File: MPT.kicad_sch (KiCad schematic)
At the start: 6 parts, among them SW1 OS102011MA1QN1

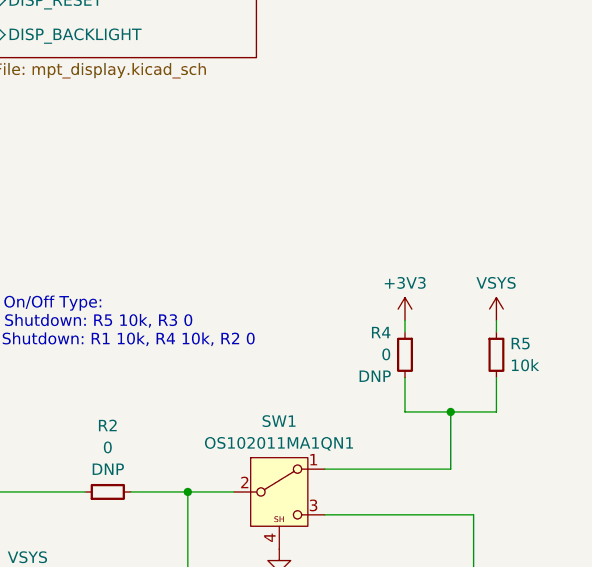
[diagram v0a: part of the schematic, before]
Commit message: Added Info-Table for STAT Pins and LEDS of Charger Work In Progress regulation for Display driving (currently not working)
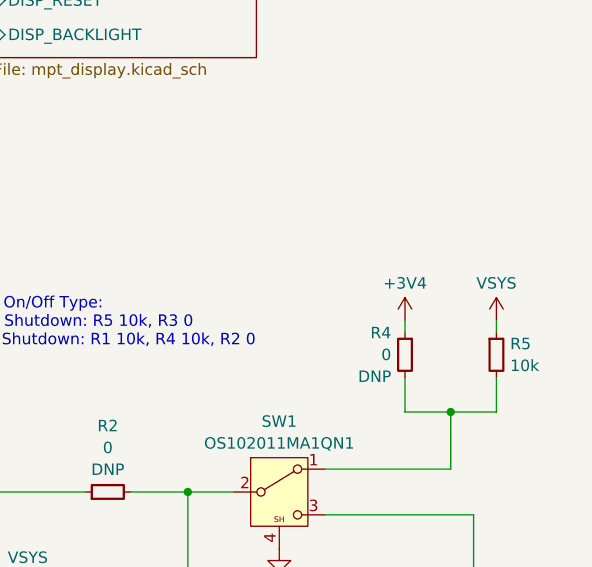
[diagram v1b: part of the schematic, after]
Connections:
- net +3V3 renamed +3V4
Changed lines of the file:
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@@
 			)
 		)
-		(property "Value" "+3V3"
+		(property "Value" "+3V4"
 			(at 228.6 86.0369 0)
 			(show_name no)

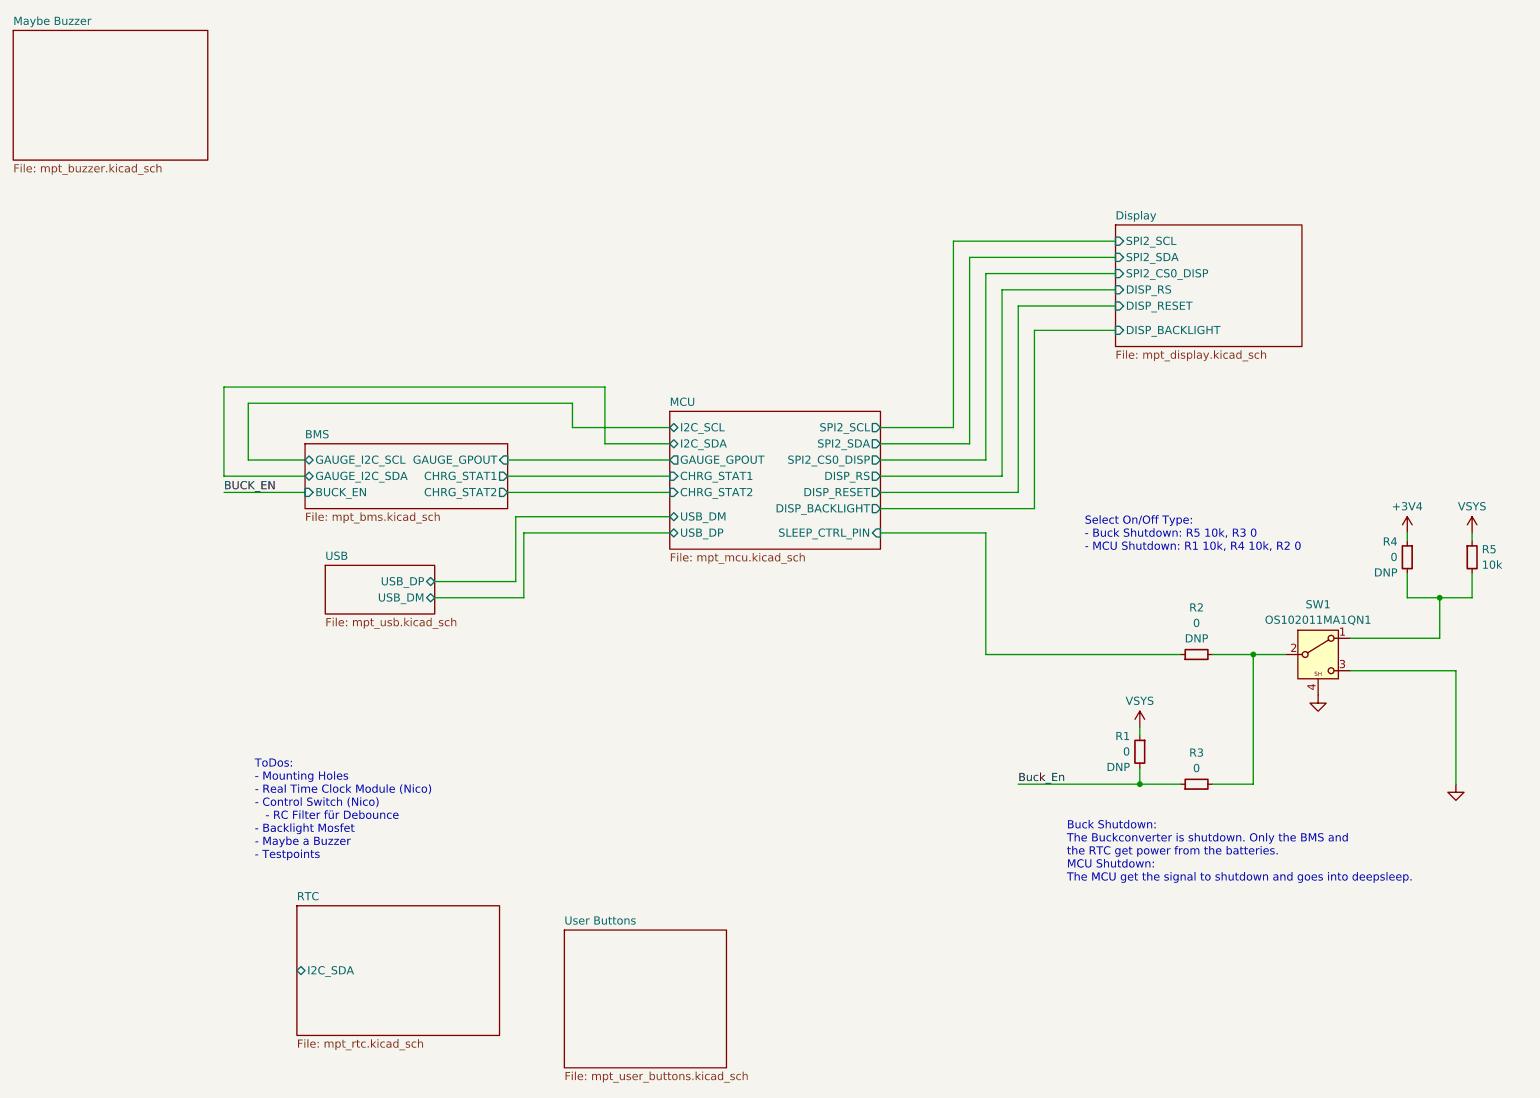
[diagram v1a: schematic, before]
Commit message: Changed LED Driver for one with lower Headroom
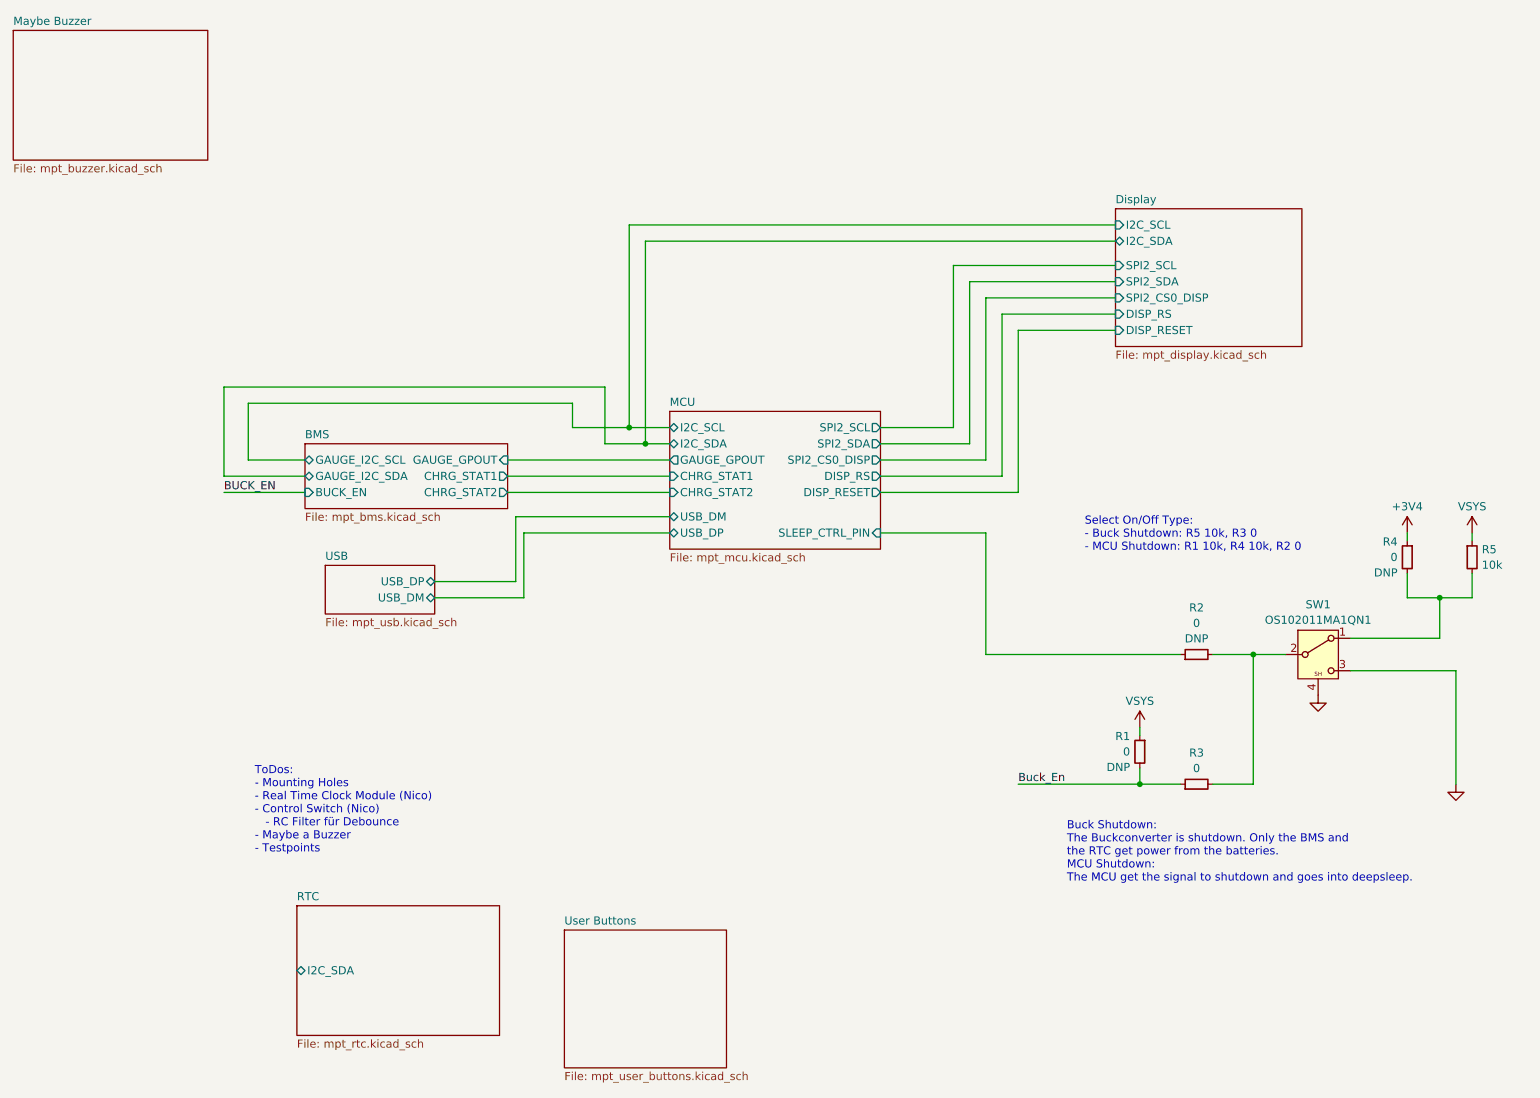
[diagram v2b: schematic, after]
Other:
- sheet Display ports: added I2C_SCL, I2C_SDA; removed DISP_BACKLIGHT
- sheet MCU ports: added none; removed DISP_BACKLIGHT
- note added: "ToDos: - Mounting Holes - Real Time Clock Module (Nico) - Control Switch (Nico) - RC Filter für Debounce - Maybe a Buzzer - Testpoints"
- note removed: "ToDos: - Mounting Holes - Real Time Clock Module (Nico) - Control Switch (Nico) - RC Filter für Debounce - Backlight Mosfet - Maybe a Buzzer - Testpoints"
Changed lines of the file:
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@@
 		)
 	)
-	(text "ToDos:\n- Mounting Holes\n- Real Time Clock Module (Nico)\n- Control Switch (Nico)\n   - RC Filter für Debounce\n- Backlight Mosfet\n- Maybe a Buzzer\n- Testpoints"
+	(text "ToDos:\n- Mounting Holes\n- Real Time Clock Module (Nico)\n- Control Switch (Nico)\n   - RC Filter für Debounce\n- Maybe a Buzzer\n- Testpoints"
 		(exclude_from_sim no)
 		(at 48.006 133.604 0)
@@
 		(color 0 0 0 0)
 	)
-	(wire
-		(pts
-			(xy 165.1 81.28) (xy 165.1 52.07)
+	(junction
+		(at 109.22 76.2)
+		(diameter 0)
+		(color 0 0 0 0)
+	)
+	(junction
+		(at 106.68 73.66)
+		(diameter 0)
+		(color 0 0 0 0)
+	)
+	(wire
+		(pts
+			(xy 165.1 81.28) (xy 165.1 55.88)
 		)
 		(stroke
@@
 	(wire
 		(pts
-			(xy 157.48 73.66) (xy 157.48 44.45)
+			(xy 157.48 73.66) (xy 157.48 48.26)
 		)
 		(stroke
@@
 	(wire
 		(pts
-			(xy 182.88 54.61) (xy 167.64 54.61)
+			(xy 182.88 58.42) (xy 167.64 58.42)
 		)
 		(stroke
@@
 	(wire
 		(pts
-			(xy 165.1 52.07) (xy 182.88 52.07)
+			(xy 165.1 55.88) (xy 182.88 55.88)
 		)
 		(stroke
@@
 	(wire
 		(pts
+			(xy 182.88 41.91) (xy 106.68 41.91)
+		)
+		(stroke
+			(width 0)
+			(type default)
+		)
+	)
+	(wire
+		(pts
 			(xy 198.12 129.54) (xy 204.47 129.54)
 		)
@@
 	(wire
 		(pts
-			(xy 162.56 78.74) (xy 162.56 49.53)
+			(xy 162.56 78.74) (xy 162.56 53.34)
 		)
 		(stroke
@@
 	(wire
 		(pts
-			(xy 160.02 46.99) (xy 182.88 46.99)
-		)
-		(stroke
-			(width 0)
-			(type default)
-		)
-	)
-	(wire
-		(pts
-			(xy 160.02 76.2) (xy 160.02 46.99)
-		)
-		(stroke
-			(width 0)
-			(type default)
-		)
-	)
-	(wire
-		(pts
-			(xy 146.05 86.36) (xy 170.18 86.36)
+			(xy 160.02 50.8) (xy 182.88 50.8)
+		)
+		(stroke
+			(width 0)
+			(type default)
+		)
+	)
+	(wire
+		(pts
+			(xy 160.02 76.2) (xy 160.02 50.8)
 		)
 		(stroke
@@
 	(wire
 		(pts
+			(xy 182.88 44.45) (xy 109.22 44.45)
+		)
+		(stroke
+			(width 0)
+			(type default)
+		)
+	)
+	(wire
+		(pts
 			(xy 186.69 127) (xy 186.69 129.54)
 		)
@@
 	(wire
 		(pts
-			(xy 157.48 44.45) (xy 182.88 44.45)
+			(xy 157.48 48.26) (xy 182.88 48.26)
 		)
 		(stroke
@@
 	(wire
 		(pts
-			(xy 167.64 54.61) (xy 167.64 83.82)
+			(xy 167.64 58.42) (xy 167.64 83.82)
 		)
 		(stroke
@@
 	(wire
 		(pts
-			(xy 170.18 58.42) (xy 182.88 58.42)
+			(xy 106.68 41.91) (xy 106.68 73.66)
 		)
 		(stroke
@@
 	(wire
 		(pts
-			(xy 162.56 49.53) (xy 182.88 49.53)
+			(xy 162.56 53.34) (xy 182.88 53.34)
 		)
 		(stroke
@@
 	(wire
 		(pts
+			(xy 109.22 44.45) (xy 109.22 76.2)
+		)
+		(stroke
+			(width 0)
+			(type default)
+		)
+	)
+	(wire
+		(pts
 			(xy 219.71 106.68) (xy 233.68 106.68)
 		)
@@
 		(pts
 			(xy 146.05 73.66) (xy 157.48 73.66)
-		)
-		(stroke
-			(width 0)
-			(type default)
-		)
-	)
-	(wire
-		(pts
-			(xy 170.18 86.36) (xy 170.18 58.42)
 		)
 		(stroke
@@
 	)
 	(sheet
-		(at 182.88 41.91)
-		(size 29.21 19.05)
+		(at 182.88 39.37)
+		(size 29.21 21.59)
 		(exclude_from_sim no)
 		(in_bom yes)
@@
 		)
 		(property "Sheetname" "Display"
-			(at 182.88 41.1984 0)
+			(at 182.88 38.6584 0)
 			(show_name no)
 			(do_not_autoplace no)
@@
 			)
 		)
-		(pin "DISP_BACKLIGHT" input
+		(pin "DISP_RESET" input
 			(at 182.88 58.42 180)
 			(effects
@@
 			)
 		)
-		(pin "DISP_RESET" input
-			(at 182.88 54.61 180)
+		(pin "DISP_RS" input
+			(at 182.88 55.88 180)
 			(effects
 				(font
@@
 			)
 		)
-		(pin "DISP_RS" input
-			(at 182.88 52.07 180)
+		(pin "SPI2_CS0_DISP" input
+			(at 182.88 53.34 180)
 			(effects
 				(font
@@
 			)
 		)
-		(pin "SPI2_CS0_DISP" input
-			(at 182.88 49.53 180)
+		(pin "SPI2_SCL" input
+			(at 182.88 48.26 180)
 			(effects
 				(font
@@
 			)
 		)
-		(pin "SPI2_SCL" input
+		(pin "SPI2_SDA" input
+			(at 182.88 50.8 180)
+			(effects
+				(font
+					(size 1.27 1.27)
+				)
+				(justify left)
+			)
+		)
+		(pin "I2C_SDA" bidirectional
 			(at 182.88 44.45 180)
 			(effects
@@
 			)
 		)
-		(pin "SPI2_SDA" input
-			(at 182.88 46.99 180)
+		(pin "I2C_SCL" input
+			(at 182.88 41.91 180)
 			(effects
 				(font
@@
 			)
 		)
-		(pin "DISP_BACKLIGHT" output
-			(at 146.05 86.36 0)
-			(effects
-				(font
-					(size 1.27 1.27)
-				)
-				(justify right)
-			)
-		)

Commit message: RTC Finished, changes to User Buttons
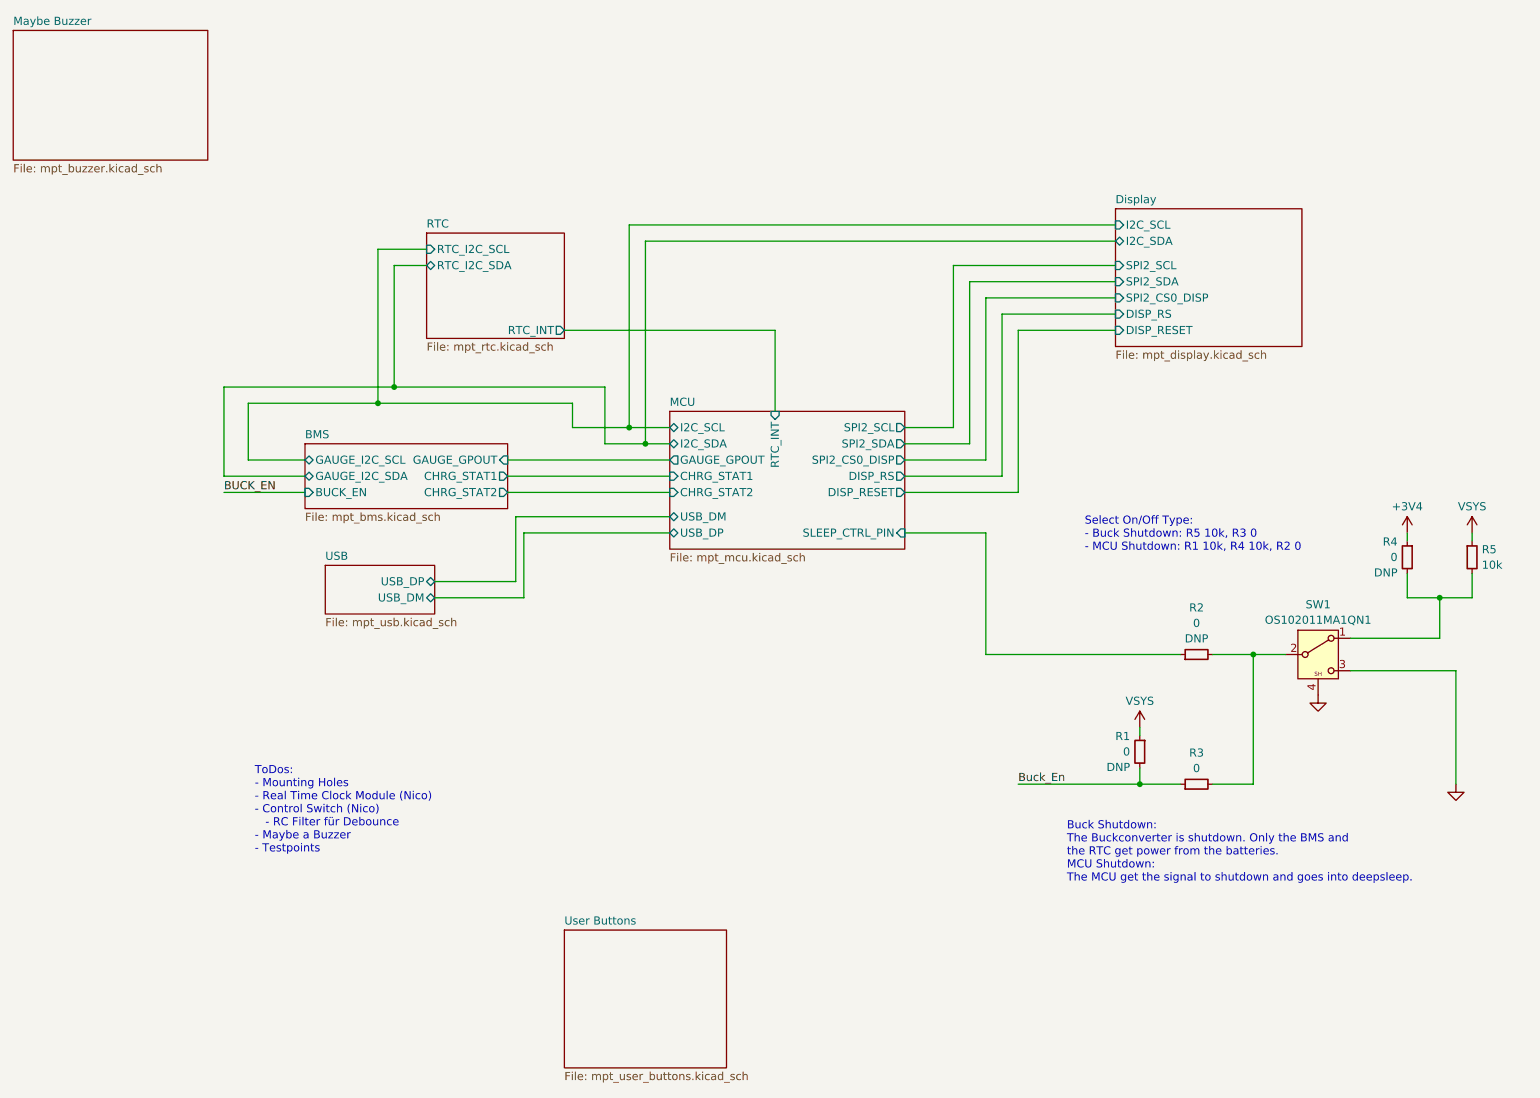
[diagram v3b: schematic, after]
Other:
- sheet MCU ports: added RTC_INT; removed none
- sheet RTC ports: added RTC_I2C_SCL, RTC_I2C_SDA, RTC_INT; removed I2C_SDA
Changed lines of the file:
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@@
 	)
 	(junction
+		(at 69.85 67.31)
+		(diameter 0)
+		(color 0 0 0 0)
+	)
+	(junction
+		(at 67.31 69.85)
+		(diameter 0)
+		(color 0 0 0 0)
+	)
+	(junction
 		(at 204.47 109.22)
 		(diameter 0)
@@
 	(wire
 		(pts
+			(xy 129.54 58.42) (xy 129.54 71.12)
+		)
+		(stroke
+			(width 0)
+			(type default)
+		)
+	)
+	(wire
+		(pts
 			(xy 204.47 129.54) (xy 204.47 109.22)
 		)
@@
 	(wire
 		(pts
+			(xy 69.85 67.31) (xy 43.18 67.31)
+		)
+		(stroke
+			(width 0)
+			(type default)
+		)
+	)
+	(wire
+		(pts
 			(xy 233.68 100.33) (xy 233.68 106.68)
 		)
@@
 	(wire
 		(pts
+			(xy 96.52 58.42) (xy 129.54 58.42)
+		)
+		(stroke
+			(width 0)
+			(type default)
+		)
+	)
+	(wire
+		(pts
+			(xy 74.93 45.72) (xy 67.31 45.72)
+		)
+		(stroke
+			(width 0)
+			(type default)
+		)
+	)
+	(wire
+		(pts
 			(xy 182.88 41.91) (xy 106.68 41.91)
 		)
@@
 	(wire
 		(pts
+			(xy 74.93 48.26) (xy 69.85 48.26)
+		)
+		(stroke
+			(width 0)
+			(type default)
+		)
+	)
+	(wire
+		(pts
 			(xy 198.12 129.54) (xy 204.47 129.54)
 		)
@@
 	(wire
 		(pts
-			(xy 97.79 69.85) (xy 46.99 69.85)
+			(xy 97.79 69.85) (xy 67.31 69.85)
 		)
 		(stroke
@@
 	(wire
 		(pts
+			(xy 67.31 45.72) (xy 67.31 69.85)
+		)
+		(stroke
+			(width 0)
+			(type default)
+		)
+	)
+	(wire
+		(pts
 			(xy 186.69 129.54) (xy 193.04 129.54)
 		)
@@
 	(wire
 		(pts
-			(xy 167.64 83.82) (xy 146.05 83.82)
+			(xy 167.64 83.82) (xy 149.86 83.82)
+		)
+		(stroke
+			(width 0)
+			(type default)
+		)
+	)
+	(wire
+		(pts
+			(xy 67.31 69.85) (xy 46.99 69.85)
 		)
 		(stroke
@@
 	(wire
 		(pts
-			(xy 146.05 90.17) (xy 162.56 90.17)
+			(xy 149.86 90.17) (xy 162.56 90.17)
 		)
 		(stroke
@@
 	(wire
 		(pts
-			(xy 102.87 67.31) (xy 43.18 67.31)
+			(xy 102.87 67.31) (xy 69.85 67.31)
 		)
 		(stroke
@@
 	(wire
 		(pts
+			(xy 69.85 48.26) (xy 69.85 67.31)
+		)
+		(stroke
+			(width 0)
+			(type default)
+		)
+	)
+	(wire
+		(pts
 			(xy 219.71 106.68) (xy 233.68 106.68)
 		)
@@
 	(wire
 		(pts
-			(xy 146.05 76.2) (xy 160.02 76.2)
+			(xy 149.86 76.2) (xy 160.02 76.2)
 		)
 		(stroke
@@
 	(wire
 		(pts
-			(xy 146.05 81.28) (xy 165.1 81.28)
+			(xy 149.86 81.28) (xy 165.1 81.28)
 		)
 		(stroke
@@
 	(wire
 		(pts
-			(xy 146.05 73.66) (xy 157.48 73.66)
+			(xy 149.86 73.66) (xy 157.48 73.66)
 		)
 		(stroke
@@
 	(wire
 		(pts
-			(xy 146.05 78.74) (xy 162.56 78.74)
+			(xy 149.86 78.74) (xy 162.56 78.74)
 		)
 		(stroke
@@
 	)
 	(sheet
-		(at 54.61 148.59)
-		(size 31.75 20.32)
+		(at 74.93 43.18)
+		(size 21.59 16.51)
 		(exclude_from_sim no)
 		(in_bom yes)
@@
 		)
 		(property "Sheetname" "RTC"
-			(at 54.61 147.8784 0)
+			(at 74.93 42.4684 0)
 			(show_name no)
 			(do_not_autoplace no)
@@
 		)
 		(property "Sheetfile" "mpt_rtc.kicad_sch"
-			(at 54.61 169.4946 0)
+			(at 74.93 60.2746 0)
 			(show_name no)
 			(do_not_autoplace no)
@@
 			)
 		)
-		(pin "I2C_SDA" bidirectional
-			(at 54.61 158.75 180)
+		(pin "RTC_I2C_SCL" input
+			(at 74.93 45.72 180)
+			(effects
+				(font
+					(size 1.27 1.27)
+				)
+				(justify left)
+			)
+		)
+		(pin "RTC_I2C_SDA" bidirectional
+			(at 74.93 48.26 180)
 			(effects
 				(font
@@
 			)
 		)
+		(pin "RTC_INT" output
+			(at 96.52 58.42 0)
+			(effects
+				(font
+					(size 1.27 1.27)
+				)
+				(justify right)
+			)
+		)
 		(instances
 			(project "MPT"
@@
 	(sheet
 		(at 113.03 71.12)
-		(size 33.02 21.59)
+		(size 36.83 21.59)
 		(exclude_from_sim no)
 		(in_bom yes)
@@
 		)
 		(pin "SPI2_CS0_DISP" output
-			(at 146.05 78.74 0)
+			(at 149.86 78.74 0)
 			(effects
 				(font
@@
 		)
 		(pin "SPI2_SCL" output
-			(at 146.05 73.66 0)
+			(at 149.86 73.66 0)
 			(effects
 				(font
@@
 		)
 		(pin "SLEEP_CTRL_PIN" input
-			(at 146.05 90.17 0)
+			(at 149.86 90.17 0)
 			(effects
 				(font
@@
 		)
 		(pin "SPI2_SDA" output
-			(at 146.05 76.2 0)
+			(at 149.86 76.2 0)
 			(effects
 				(font
@@
 		)
 		(pin "DISP_RESET" output
-			(at 146.05 83.82 0)
+			(at 149.86 83.82 0)
 			(effects
 				(font
@@
 		)
 		(pin "DISP_RS" output
-			(at 146.05 81.28 0)
+			(at 149.86 81.28 0)
+			(effects
+				(font
+					(size 1.27 1.27)
+				)
+				(justify right)
+			)
+		)
+		(pin "RTC_INT" input
+			(at 129.54 71.12 90)
 			(effects
 				(font
